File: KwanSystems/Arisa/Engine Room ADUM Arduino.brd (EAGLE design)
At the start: 61 x 43.2 mm, 50 parts, among them J001 USB_MICROB_JSTGCT, J002 M15, J003 M15, Q201 MOSFET_NCHANNELIRF6718, Q202 MOSFET_NCHANNELIRF6718, U001 FT232RLSSOP, U201 L298, U202 PC847, U203 MC74VHC1G04, U204 UA78M05, U401 ATMEGA328P

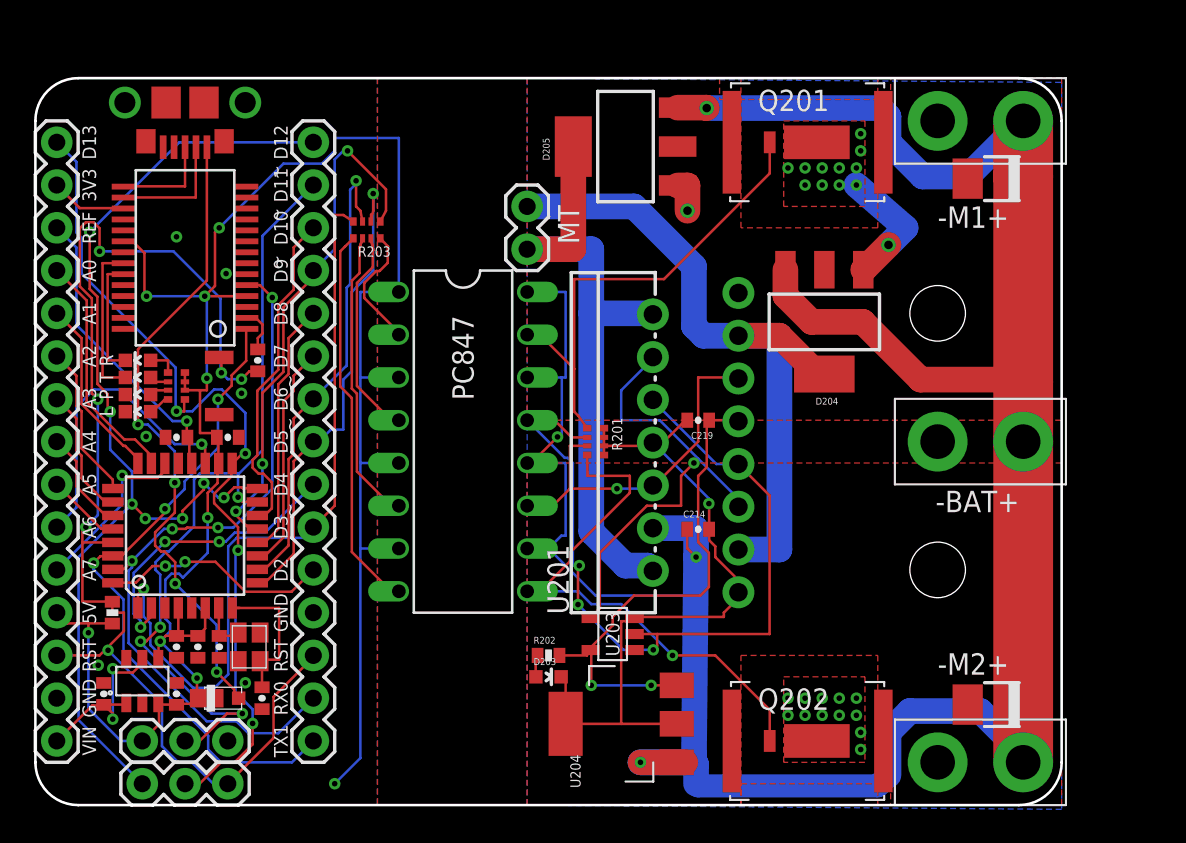
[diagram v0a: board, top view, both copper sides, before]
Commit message: Reorganized docs for ARM. Added engine rooms with AD magnetic couplers instead of optocouplers.
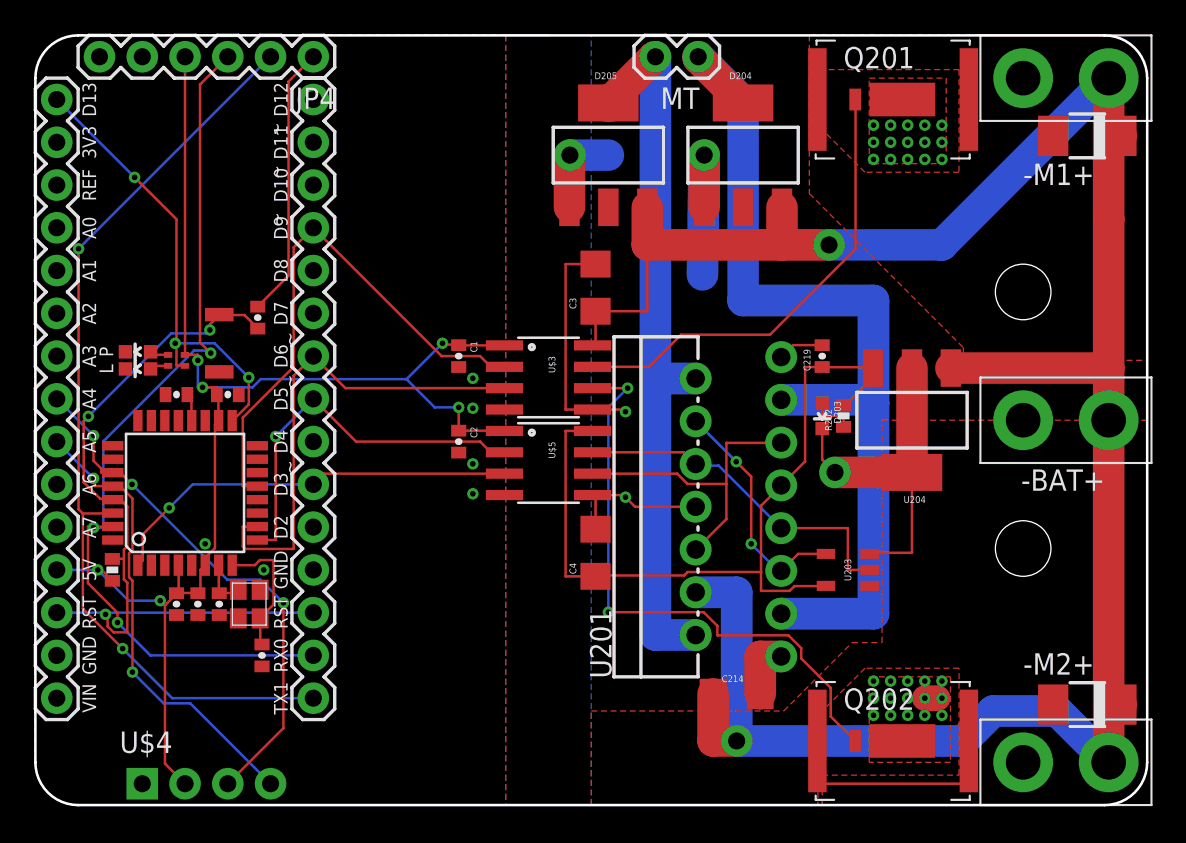
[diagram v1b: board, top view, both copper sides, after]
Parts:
- removed C002: 100nF, SparkFun:0402-CAP
- removed C201: 1uF, SparkFun:0402-CAP
- removed C203: 4.7uF, SparkFun:0402-CAP
- removed D003: MSS1P6, KwanSystems:MICROSMP
- removed D022: BLUE, SparkFun-LED:LED-0603
- removed D023: RED, SparkFun-LED:LED-0603
- removed J001: USB_MICROB_JSTGCT, KwanSystems:USB_MICROB_3075
- removed JP3: (no value), SparkFun-Connectors:1X03
- removed R201: 1k, KwanSystems:CRA04
- removed R203: 220, KwanSystems:CRA04
- removed U001: FT232RLSSOP, SparkFun-DigitalIC:SSOP28DB
- removed U002: (no value), KwanSystems:SOT-23-6
- removed U202: PC847, optocoupler:DIL16
- added C005, C1, C2: 100nF, SparkFun:0402-CAP
- added C3, C4: 10uF, SparkFun-Passives:1206
- added U$4: M04NOSILK, KwanSystems:M04SIP
- added U$5: ADUM3221, KwanSystems:SO8N
- added Y401: 8MHz, KwanSystems:CRYSTAL_SMD_2MM_2_5MM
- C214: device SparkFun:0402-CAP -> SparkFun-Passives:1206
- JP4: device SparkFun-Connectors:1X03 -> SparkFun-Connectors:1X06
- R001: device KwanSystems:CRA04 -> KwanSystems:CRA02
- U$3: value (none) -> ADUM3221; device KwanSystems:CRYSTAL_SMD_2MM_2_5MM -> KwanSystems:SO8N
- U204: device MySMD:SOT223 -> KwanSystems:SOT-223
- moved JP4 41.0 mm to (16.5, 44.5)
- moved U204 24.7 mm to (52.1, 22.9), turned to 180 degrees
- moved U$3 23.9 mm to (30.5, 25.4)
- moved R202 22.6 mm to (48.0, 23.1), turned to 90 degrees
- moved D203 22.5 mm to (46.7, 23.1), turned to 180 degrees
- moved U203 14.5 mm to (48.3, 14.0)
- moved MT 13.5 mm to (39.4, 44.5), turned to 180 degrees
- moved U$2 13.3 mm to (34.3, 4.32)
- moved D204 11.0 mm to (42.0, 38.6), turned to 0 degrees
- moved C214 10.0 mm to (41.7, 6.60)
- moved C219 8.29 mm to (46.7, 26.7), turned to 90 degrees
- moved D201 5.68 mm to (62.5, 39.8)
- moved M1 5.68 mm to (61.2, 43.2)
- moved Q201 5.68 mm to (50.8, 41.9)
- moved BAT 5.24 mm to (61.2, 22.9)
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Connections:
- removed net 3V3: J003.2, U001.17
- removed net A0: J003.4, U401.23
- removed net A1: J003.5, U401.24
- removed net A2: J003.6, U401.25
- removed net A3: J003.7, U401.26
- removed net A4: J003.8, U401.27
- removed net A5: J003.9, U401.28
- removed net A6: J003.10, U401.19
- removed net A7: J003.11, U401.22
- removed net D10: J002.13, U401.14
- removed net D11: J002.14, JP4.2, U401.15
- removed net D12: J002.15, JP3.1, U401.16
- removed net D2: J002.5, U401.32
- removed net D3_ISO: R203.5, U202.8
- removed net D4: J002.7, U401.2
- removed net D5_ISO: R203.7, U202.4
- removed net D6_ISO: R203.6, U202.6
- removed net D7: J002.10, U401.11
- removed net D8: J002.11, U401.12
- removed net D9_ISO: R203.8, U202.2
- removed net N$10: C219.1, R202.2, U201.9, U203.5, U204.3
- removed net N$11: D023.A, R001.1
- removed net N$28: R201.3, U201.11, U201.6, U202.11
- removed net N$35: Q201.G, R201.1, U202.15
- removed net N$36: Q202.G, R201.4, U202.9
- removed net N$37: R201.2, U201.10, U201.7, U202.13, U203.2
- removed net N$5: J001.3, U001.15
- removed net N$6: J001.2, U001.16
- removed net N$9: D022.A, R001.2
- removed net RXLED1: D022.C, U001.22
- removed net TXLED1: D023.C, U001.23
- removed net VBUS: D003.A, J001.1
- removed net VIN: C201.1, J003.15, U002.1, U002.5
- new net A4/SDA: J003.8, U$4.3, U401.27
- new net A5/SCL: J003.9, U$4.4, U401.28
- new net M1_PWM_O: Q201.G, U$3.7
- new net M2_PWM_O: Q202.G, U$3.6
- new net MT_DIR_O: U$5.7, U201.10, U201.7, U203.2
- new net MT_PWM_O: U$5.6, U201.11, U201.6
- new net PVCC: C219.1, C4.1, R202.2, U$5.8, U201.9, U203.5, U204.3
- net AREF: no longer J003.3
- net D0: now also JP4.2; no longer U001.1
- net D1: now also JP4.3; no longer U001.5
- net D13: now also R001.3; no longer JP3.2, R001.5
- net D3: now also U$5.3; no longer R203.4
- net D5: now also U$5.2; no longer R203.2
- net D6: now also U$3.3; no longer R203.3
- net D9: now also U$3.2; no longer R203.1
- net DTR#: now also C005.2, JP4.1; no longer C002.2, U001.2
- net GND: now also C1.2, C2.2, JP4.5, JP4.6, U$4.1, U$5.4, Y401.2, Y401.4; no longer C201.2, C203.2, J001.5, J001.P$1, J001.P$10, J001.P$2, J001.P$3, J001.P$4, J001.P$8, JP4.1, U$3.2, U001.18, U001.21, U001.25, U001.26, U001.7, U002.2
- net N$3: now also Y401.1; no longer U$3.1
- net N$4: now also Y401.3; no longer U$3.3
- net N$7: now also R001.1; no longer R001.3
- net N$8: now also R001.2; no longer R001.4
- net PGND: now also C3.2, C4.2, U$3.5, U$5.5; no longer R201.5, R201.6, R201.7, R201.8
- net RESET: now also C005.1; no longer C002.1, JP3.3
- net VCC: now also C1.1, C2.1, JP4.4, R001.4, U$3.1, U$4.2, U$5.1; no longer C203.1, D003.K, JP4.3, R001.6, R001.7, R001.8, U001.20, U001.4, U002.3, U002.4, U202.1, U202.3, U202.5, U202.7
- net VDD: now also C3.1, U$3.8; no longer U202.10, U202.12, U202.14, U202.16
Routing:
- net D12: track 62.1 -> 0.00 mm, vias 7 -> 0
- net VCC: track 134.8 -> 84.9 mm, vias 9 -> 6
- net N$37: track 48.8 -> 0.00 mm, vias 3 -> 0
- net D11: track 47.9 -> 0.00 mm, vias 4 -> 0
- net PVCC: track 0.00 -> 47.5 mm
- net VBUS: track 38.7 -> 0.00 mm, vias 4 -> 0
- net VDD: track 180.1 -> 142.5 mm, vias 4 -> 2
- net M2_PWM_O: track 0.00 -> 35.4 mm, vias 0 -> 2
- net N$36: track 32.9 -> 0.00 mm, vias 1 -> 0
- net A4/SDA: track 0.00 -> 31.6 mm, vias 0 -> 3
- net N$10: track 30.5 -> 0.00 mm, vias 2 -> 0
- net N$35: track 29.0 -> 0.00 mm
- net RESET: track 74.5 -> 46.1 mm, vias 6 -> 3
- net A5/SCL: track 0.00 -> 27.6 mm, vias 0 -> 2
- net M1_PWM_O: track 0.00 -> 27.4 mm
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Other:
- board size 61 x 43.2 mm -> 66 x 45.7 mm
- board text added: "1 Apr 2014"
- board text added: "LPC2148 Engine Room"
- board text removed: "5 Aug 2011"
- board text removed: "Arduino Engine Room"
- board text removed: "R"
- board text removed: "T"
